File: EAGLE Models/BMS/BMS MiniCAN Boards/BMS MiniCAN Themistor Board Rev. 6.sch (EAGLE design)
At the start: 111 parts, among them IC1 AT90CAN128, IC2 MCP2551SO8, IC3 NUP2105L, IC4 LM117MPX-5.0, IC5 CD74HC4067, IC6 CD74HC4067, IC7 CD74HC4067, IC8 CD74HC4067, X1 10127720-241LF, X2 10127720-241LF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

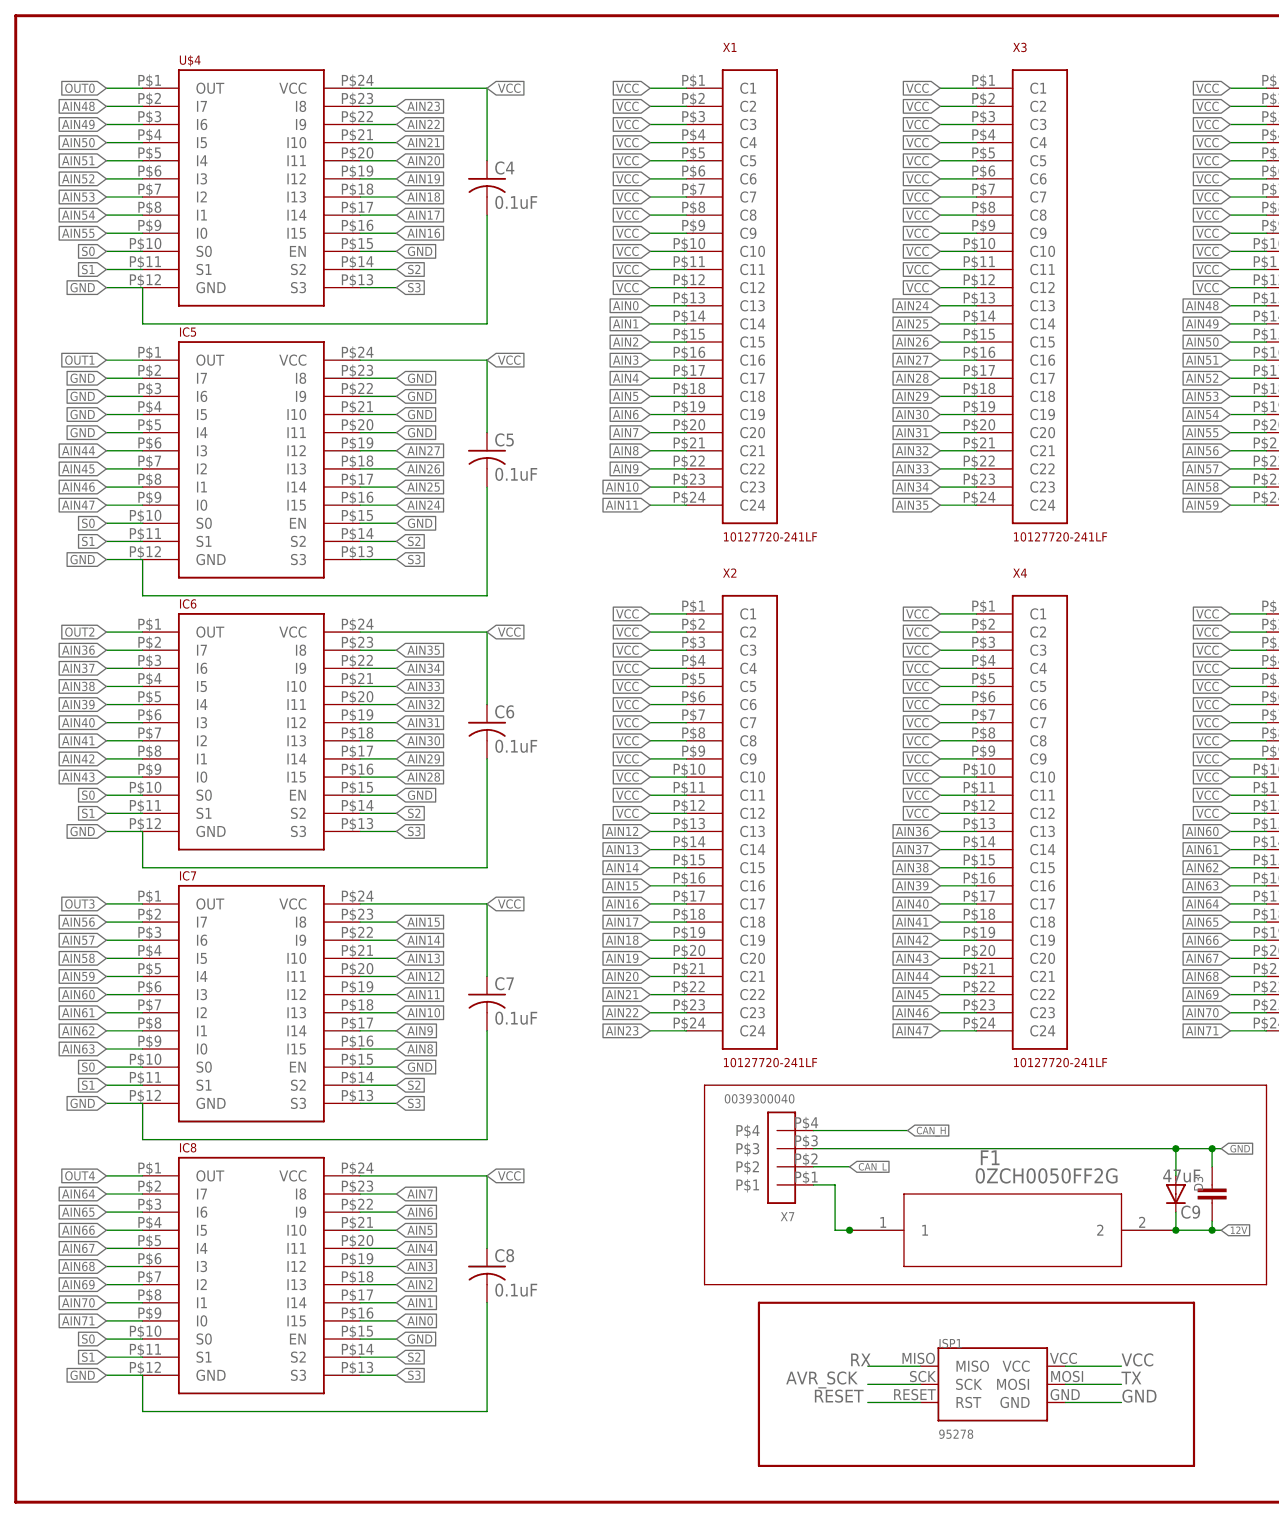
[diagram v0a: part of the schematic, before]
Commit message: Changed various things
Changed hole sizes, rearranged protection circuit, changed mosi miso on
6 pin header, moved 6 pin header farther away from AT90, deleted
redundant protection diode, created better spacing for CAN protection
IC, added credits.
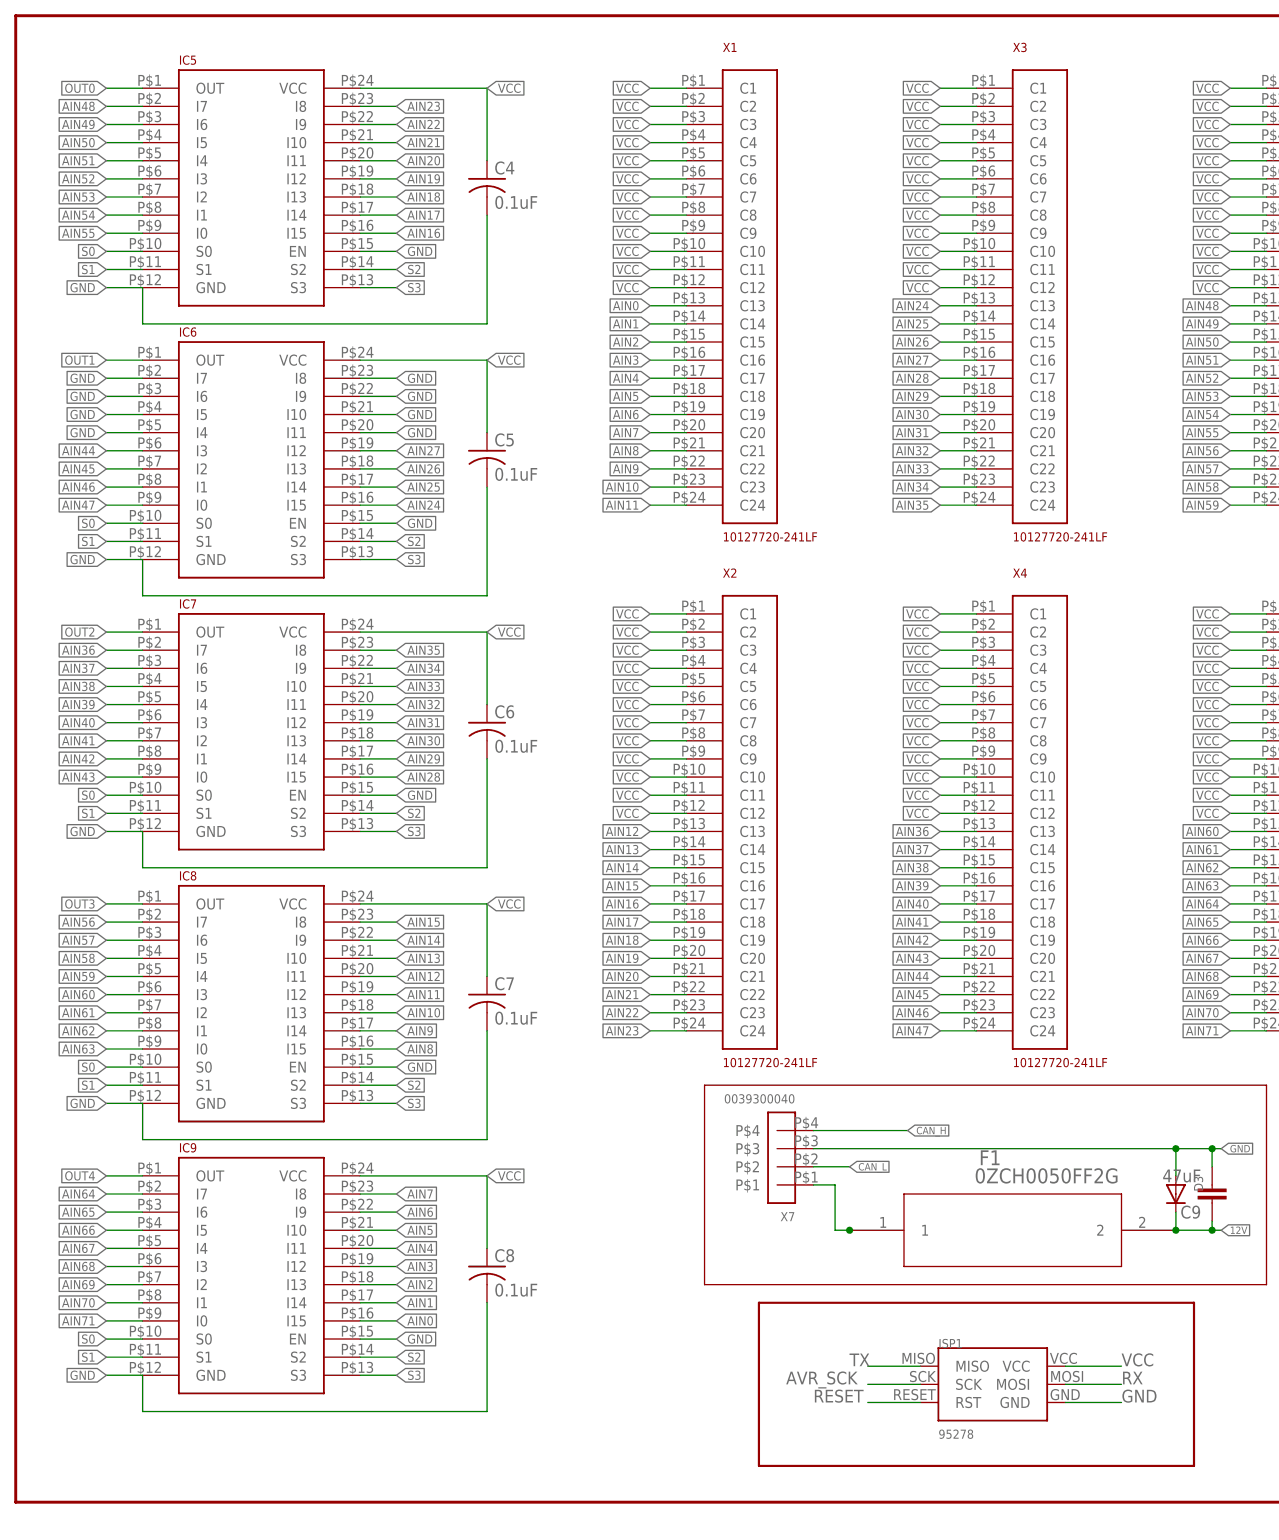
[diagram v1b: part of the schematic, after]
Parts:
- removed U$4: CD74HC4067, BMS Lbr:CD74HC4067
- added IC9: CD74HC4067, BMS Lbr:CD74HC4067
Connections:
- net AIN0: now also IC9.I15; no longer IC8.I15
- net AIN1: now also IC9.I14; no longer IC8.I14
- net AIN10: now also IC8.I13; no longer IC7.I13
- net AIN11: now also IC8.I12; no longer IC7.I12
- net AIN12: now also IC8.I11; no longer IC7.I11
- net AIN13: now also IC8.I10; no longer IC7.I10
- net AIN14: now also IC8.I9; no longer IC7.I9
- net AIN15: now also IC8.I8; no longer IC7.I8
- net AIN16: now also IC5.I15; no longer U$4.I15
- net AIN17: now also IC5.I14; no longer U$4.I14
- net AIN18: now also IC5.I13; no longer U$4.I13
- net AIN19: now also IC5.I12; no longer U$4.I12
- net AIN2: now also IC9.I13; no longer IC8.I13
- net AIN20: now also IC5.I11; no longer U$4.I11
- net AIN21: now also IC5.I10; no longer U$4.I10
- net AIN22: now also IC5.I9; no longer U$4.I9
- net AIN23: now also IC5.I8; no longer U$4.I8
- net AIN24: now also IC6.I15; no longer IC5.I15
- net AIN25: now also IC6.I14; no longer IC5.I14
- net AIN26: now also IC6.I13; no longer IC5.I13
- net AIN27: now also IC6.I12; no longer IC5.I12
- net AIN28: now also IC7.I15; no longer IC6.I15
- net AIN29: now also IC7.I14; no longer IC6.I14
- net AIN3: now also IC9.I12; no longer IC8.I12
- net AIN30: now also IC7.I13; no longer IC6.I13
- net AIN31: now also IC7.I12; no longer IC6.I12
- net AIN32: now also IC7.I11; no longer IC6.I11
- net AIN33: now also IC7.I10; no longer IC6.I10
- net AIN34: now also IC7.I9; no longer IC6.I9
- net AIN35: now also IC7.I8; no longer IC6.I8
- net AIN36: now also IC7.I7; no longer IC6.I7
- net AIN37: now also IC7.I6; no longer IC6.I6
- net AIN38: now also IC7.I5; no longer IC6.I5
- net AIN39: now also IC7.I4; no longer IC6.I4
- net AIN4: now also IC9.I11; no longer IC8.I11
- net AIN40: now also IC7.I3; no longer IC6.I3
- net AIN41: now also IC7.I2; no longer IC6.I2
- net AIN42: now also IC7.I1; no longer IC6.I1
- net AIN43: now also IC7.I0; no longer IC6.I0
- net AIN44: now also IC6.I3; no longer IC5.I3
- net AIN45: now also IC6.I2; no longer IC5.I2
- net AIN46: now also IC6.I1; no longer IC5.I1
- net AIN47: now also IC6.I0; no longer IC5.I0
- net AIN48: now also IC5.I7; no longer U$4.I7
- net AIN49: now also IC5.I6; no longer U$4.I6
- net AIN5: now also IC9.I10; no longer IC8.I10
- net AIN50: now also IC5.I5; no longer U$4.I5
- net AIN51: now also IC5.I4; no longer U$4.I4
- net AIN52: now also IC5.I3; no longer U$4.I3
- net AIN53: now also IC5.I2; no longer U$4.I2
- net AIN54: now also IC5.I1; no longer U$4.I1
- net AIN55: now also IC5.I0; no longer U$4.I0
- net AIN56: now also IC8.I7; no longer IC7.I7
- net AIN57: now also IC8.I6; no longer IC7.I6
- net AIN58: now also IC8.I5; no longer IC7.I5
- net AIN59: now also IC8.I4; no longer IC7.I4
- net AIN6: now also IC9.I9; no longer IC8.I9
- net AIN60: now also IC8.I3; no longer IC7.I3
- net AIN61: now also IC8.I2; no longer IC7.I2
- net AIN62: now also IC8.I1; no longer IC7.I1
- net AIN63: now also IC8.I0; no longer IC7.I0
- net AIN64: now also IC9.I7; no longer IC8.I7
- net AIN65: now also IC9.I6; no longer IC8.I6
- net AIN66: now also IC9.I5; no longer IC8.I5
- net AIN67: now also IC9.I4; no longer IC8.I4
- net AIN68: now also IC9.I3; no longer IC8.I3
- net AIN69: now also IC9.I2; no longer IC8.I2
- net AIN7: now also IC9.I8; no longer IC8.I8
- net AIN70: now also IC9.I1; no longer IC8.I1
- net AIN71: now also IC9.I0; no longer IC8.I0
- net AIN8: now also IC8.I15; no longer IC7.I15
- net AIN9: now also IC8.I14; no longer IC7.I14
- net GND: now also IC6.I10, IC6.I11, IC6.I4, IC6.I5, IC6.I6, IC6.I7, IC6.I8, IC6.I9, IC9.EN, IC9.GND; no longer IC5.I10, IC5.I11, IC5.I4, IC5.I5, IC5.I6, IC5.I7, IC5.I8, IC5.I9, U$4.EN, U$4.GND
- net OUT0: now also IC5.OUT; no longer U$4.OUT
- net OUT1: now also IC6.OUT; no longer IC5.OUT
- net OUT2: now also IC7.OUT; no longer IC6.OUT
- net OUT3: now also IC8.OUT; no longer IC7.OUT
- net OUT4: now also IC9.OUT; no longer IC8.OUT
- net RX: now also ISP1.MOSI; no longer ISP1.MISO
- net S0: now also IC9.S0; no longer U$4.S0
- net S1: now also IC9.S1; no longer U$4.S1
- net S2: now also IC9.S2; no longer U$4.S2
- net S3: now also IC9.S3; no longer U$4.S3
- net TX: now also ISP1.MISO; no longer ISP1.MOSI
- net VCC: now also IC9.VCC; no longer U$4.VCC
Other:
- moved on the sheet: IC5, IC6, IC7, IC8
